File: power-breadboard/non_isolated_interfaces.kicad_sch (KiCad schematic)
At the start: 9 parts

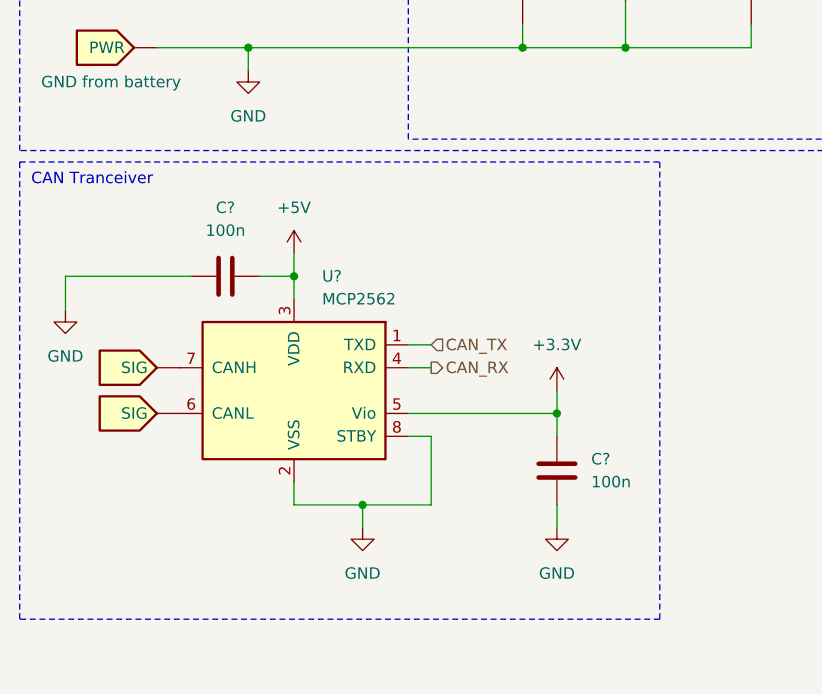
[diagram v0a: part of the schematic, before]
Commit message: power-pcb: add imd input to safety systems page
Use the same CAN transceiver as for the network since it also supports
24V-CAN. Also re-added a separate 24V input for the contactors.
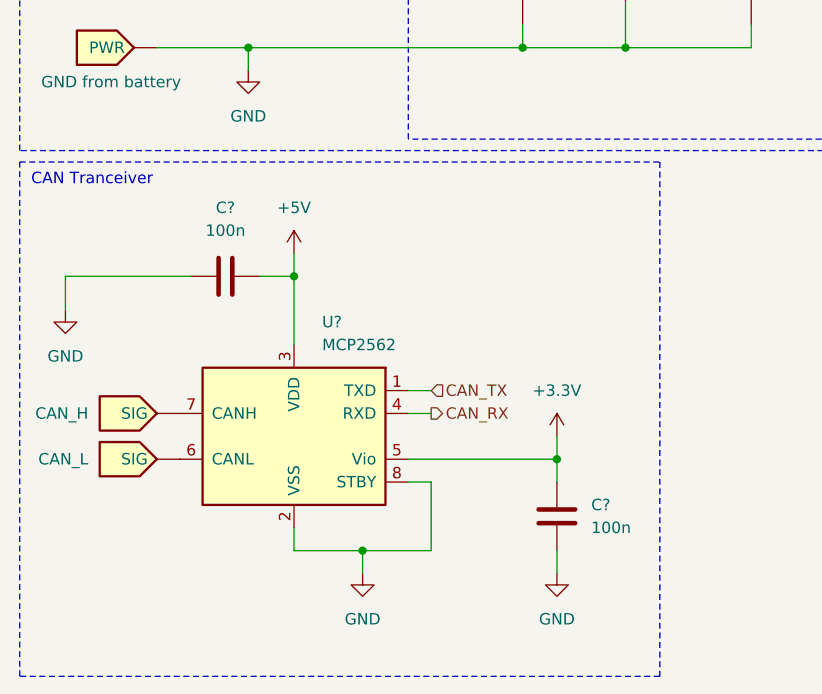
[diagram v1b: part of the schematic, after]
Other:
- moved on the sheet: C?, U?

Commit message: power-breadboard: annotate whole schematic
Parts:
- gave numbers to parts that had none: 8
- renumbered F3 to F2
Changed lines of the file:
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@@
 		(in_pos_files yes)
 		(dnp no)
-		(property "Reference" "F3"
+		(property "Reference" "F2"
 			(at 144.78 27.94 90)
 			(show_name no)
@@
 			(project "power-breadboard"
 				(path "/4b4cf3aa-c94c-4150-b9c5-35049cd71136/d2b1a814-a8ab-491d-a39f-63fa9799b0cb"
-					(reference "F3")
+					(reference "F2")
 					(unit 1)
 					(variant
@@
 		(in_pos_files yes)
 		(dnp no)
-		(property "Reference" "J?"
+		(property "Reference" "J1"
 			(at 163.83 31.75 0)
 			(show_name no)
@@
 			(project "power-breadboard"
 				(path "/4b4cf3aa-c94c-4150-b9c5-35049cd71136/d2b1a814-a8ab-491d-a39f-63fa9799b0cb"
-					(reference "J?")
+					(reference "J1")
 					(unit 1)
 				)
@@
 		(dnp no)
 		(fields_autoplaced yes)
-		(property "Reference" "#PWR02"
+		(property "Reference" "#PWR05"
 			(at 38.1 48.26 0)
 			(hide yes)
@@
 			(project "power-breadboard"
 				(path "/4b4cf3aa-c94c-4150-b9c5-35049cd71136/d2b1a814-a8ab-491d-a39f-63fa9799b0cb"
-					(reference "#PWR02")
+					(reference "#PWR05")
 					(unit 1)
 				)
@@
 		(in_pos_files yes)
 		(dnp no)
-		(property "Reference" "C?"
+		(property "Reference" "C2"
 			(at 97.79 30.8609 0)
 			(show_name no)
@@
 			(project "power-breadboard"
 				(path "/4b4cf3aa-c94c-4150-b9c5-35049cd71136/d2b1a814-a8ab-491d-a39f-63fa9799b0cb"
-					(reference "C?")
+					(reference "C2")
 					(unit 1)
 				)
@@
 		(dnp no)
 		(fields_autoplaced yes)
-		(property "Reference" "#PWR06"
+		(property "Reference" "#PWR09"
 			(at 50.8 104.14 0)
 			(hide yes)
@@
 			(project "power-breadboard"
 				(path "/4b4cf3aa-c94c-4150-b9c5-35049cd71136/d2b1a814-a8ab-491d-a39f-63fa9799b0cb"
-					(reference "#PWR06")
+					(reference "#PWR09")
 					(unit 1)
 				)
@@
 		(dnp no)
 		(fields_autoplaced yes)
-		(property "Reference" "C?"
+		(property "Reference" "C3"
 			(at 35.56 57.15 90)
 			(show_name no)
@@
 			(project "power-breadboard"
 				(path "/4b4cf3aa-c94c-4150-b9c5-35049cd71136/d2b1a814-a8ab-491d-a39f-63fa9799b0cb"
-					(reference "C?")
+					(reference "C3")
 					(unit 1)
 				)
@@
 		(in_pos_files yes)
 		(dnp no)
-		(property "Reference" "C?"
+		(property "Reference" "C1"
 			(at 64.77 30.8609 0)
 			(show_name no)
@@
 			(project "power-breadboard"
 				(path "/4b4cf3aa-c94c-4150-b9c5-35049cd71136/d2b1a814-a8ab-491d-a39f-63fa9799b0cb"
-					(reference "C?")
+					(reference "C1")
 					(unit 1)
 				)
@@
 		(dnp no)
 		(fields_autoplaced yes)
-		(property "Reference" "C?"
+		(property "Reference" "C4"
 			(at 76.2 90.1699 0)
 			(show_name no)
@@
 			(project "power-breadboard"
 				(path "/4b4cf3aa-c94c-4150-b9c5-35049cd71136/d2b1a814-a8ab-491d-a39f-63fa9799b0cb"
-					(reference "C?")
+					(reference "C4")
 					(unit 1)
 				)
@@
 		(dnp no)
 		(fields_autoplaced yes)
-		(property "Reference" "#PWR09"
+		(property "Reference" "#PWR06"
 			(at 43.18 66.04 0)
 			(hide yes)
@@
 			(project "power-breadboard"
 				(path "/4b4cf3aa-c94c-4150-b9c5-35049cd71136/d2b1a814-a8ab-491d-a39f-63fa9799b0cb"
-					(reference "#PWR09")
+					(reference "#PWR06")
 					(unit 1)
 				)
@@
 		(dnp no)
 		(fields_autoplaced yes)
-		(property "Reference" "#PWR05"
+		(property "Reference" "#PWR04"
 			(at 152.4 43.18 0)
 			(hide yes)
@@
 			(project "power-breadboard"
 				(path "/4b4cf3aa-c94c-4150-b9c5-35049cd71136/d2b1a814-a8ab-491d-a39f-63fa9799b0cb"
-					(reference "#PWR05")
+					(reference "#PWR04")
 					(unit 1)
 				)
@@
 		(dnp no)
 		(fields_autoplaced yes)
-		(property "Reference" "#PWR03"
+		(property "Reference" "#PWR02"
 			(at 100.33 27.94 0)
 			(hide yes)
@@
 			(project "power-breadboard"
 				(path "/4b4cf3aa-c94c-4150-b9c5-35049cd71136/d2b1a814-a8ab-491d-a39f-63fa9799b0cb"
-					(reference "#PWR03")
+					(reference "#PWR02")
 					(unit 1)
 				)
@@
 		(dnp no)
 		(fields_autoplaced yes)
-		(property "Reference" "U?"
+		(property "Reference" "U1"
 			(at 80.01 20.32 0)
 			(show_name no)
@@
 			(project "power-breadboard"
 				(path "/4b4cf3aa-c94c-4150-b9c5-35049cd71136/d2b1a814-a8ab-491d-a39f-63fa9799b0cb"
-					(reference "U?")
+					(reference "U1")
 					(unit 1)
 				)
@@
 		(dnp no)
 		(fields_autoplaced yes)
-		(property "Reference" "#PWR08"
+		(property "Reference" "#PWR010"
 			(at 72.39 104.14 0)
 			(hide yes)
@@
 			(project "power-breadboard"
 				(path "/4b4cf3aa-c94c-4150-b9c5-35049cd71136/d2b1a814-a8ab-491d-a39f-63fa9799b0cb"
-					(reference "#PWR08")
+					(reference "#PWR010")
 					(unit 1)
 				)
@@
 		(dnp no)
 		(fields_autoplaced yes)
-		(property "Reference" "U?"
+		(property "Reference" "U2"
 			(at 46.2981 69.85 0)
 			(show_name no)
@@
 			(project "power-breadboard"
 				(path "/4b4cf3aa-c94c-4150-b9c5-35049cd71136/d2b1a814-a8ab-491d-a39f-63fa9799b0cb"
-					(reference "U?")
+					(reference "U2")
 					(unit 1)
 				)
@@
 		(dnp no)
 		(fields_autoplaced yes)
-		(property "Reference" "#PWR07"
+		(property "Reference" "#PWR08"
 			(at 72.39 86.36 0)
 			(hide yes)
@@
 			(project "power-breadboard"
 				(path "/4b4cf3aa-c94c-4150-b9c5-35049cd71136/d2b1a814-a8ab-491d-a39f-63fa9799b0cb"
-					(reference "#PWR07")
+					(reference "#PWR08")
 					(unit 1)
 				)
@@
 		(in_pos_files yes)
 		(dnp no)
-		(property "Reference" "#PWR023"
+		(property "Reference" "#PWR03"
 			(at 137.16 30.48 0)
 			(hide yes)
@@
 			(project "power-breadboard"
 				(path "/4b4cf3aa-c94c-4150-b9c5-35049cd71136/d2b1a814-a8ab-491d-a39f-63fa9799b0cb"
-					(reference "#PWR023")
+					(reference "#PWR03")
 					(unit 1)
 				)
@@
 		(in_pos_files yes)
 		(dnp no)
-		(property "Reference" "F?"
+		(property "Reference" "F1"
 			(at 43.18 20.32 90)
 			(show_name no)
@@
 			(project "power-breadboard"
 				(path "/4b4cf3aa-c94c-4150-b9c5-35049cd71136/d2b1a814-a8ab-491d-a39f-63fa9799b0cb"
-					(reference "F?")
+					(reference "F1")
 					(unit 1)
 					(variant
@@
 		(dnp no)
 		(fields_autoplaced yes)
-		(property "Reference" "#PWR010"
+		(property "Reference" "#PWR07"
 			(at 17.78 74.93 0)
 			(hide yes)
@@
 			(project "power-breadboard"
 				(path "/4b4cf3aa-c94c-4150-b9c5-35049cd71136/d2b1a814-a8ab-491d-a39f-63fa9799b0cb"
-					(reference "#PWR010")
-					(unit 1)
-				)
+					(reference "#PWR07")
+					(unit 1)
+				)
